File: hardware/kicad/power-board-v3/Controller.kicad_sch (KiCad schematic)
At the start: 1 part

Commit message: initial controller design
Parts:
- added C?: 10uF, symbol Device:C_Small
- added C? (x3): 100nF, symbol Device:C_Small
- added C?: 1uF, symbol Device:C_Small
- added J?: USB_BREAKOUT, Connector_PinHeader_2.54mm:PinHeader_1x03_P2.54mm_Vertical, symbol Connector_Generic:Conn_01x03
- added J?: SERIAL_PROGRAMMING, Connector_PinHeader_2.54mm:PinHeader_1x06_P2.54mm_Vertical, symbol Connector_Generic:Conn_01x06
- added J?: Conn_ARM_JTAG_SWD_10, Connector:Tag-Connect_TC2050-IDC-FP_2x05_P1.27mm_Vertical, symbol Connector:Conn_ARM_JTAG_SWD_10
- added JP?: JTAG_SELECT, symbol Jumper:SolderJumper_3_Open
- added Q? (x2): L8050QLT1G, Package_TO_SOT_SMD:SOT-23, symbol Device:Q_NPN_BEC
- added R? (x9): 10K, symbol Device:R_Small
- added SW?: BOOT, Button_Switch_SMD:SW_SPST_TL3342, symbol Switch:SW_Push
- added SW?: RESET, Button_Switch_SMD:SW_SPST_TL3342, symbol Switch:SW_Push
- added U?: ESP32-S3-MINI-1, Espressif:ESP32-S3-MINI-1, symbol Espressif:ESP32-S3-MINI-1
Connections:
- net +3.3v: now also C?.1, C?.1, J?.1 (VTref), R?.1, R?.2, R?.2, R?.2, U?.3 (3V3)
- net EN_FAN: now also U?.11 (GPIO7/TOUCH7/ADC1_CH6)
- net EN_LORA: now also U?.8 (GPIO4/TOUCH4/ADC1_CH3)
- net EN_RPI: now also U?.10 (GPIO6/TOUCH6/ADC1_CH5)
- net EN_SWARM: now also U?.9 (GPIO5/TOUCH5/ADC1_CH4)
- net GND: now also C?.2, C?.2, C?.2, C?.2, C?.2, J?.1 (Pin_1), J?.3 (GND), J?.5 (GND), J?.6 (Pin_6), J?.9 (GNDDetect), R?.1, R?.1, R?.1, SW?.1, SW?.1, U?.1 (GND), U?.2 (GND), U?.42 (GND), U?.43 (GND), U?.46 (GND), U?.47 (GND), U?.48 (GND), U?.49 (GND), U?.50 (GND), U?.51 (GND), U?.52 (GND), U?.53 (GND), U?.54 (GND), U?.55 (GND), U?.56 (GND), U?.57 (GND), U?.58 (GND), U?.59 (GND), U?.60 (GND), U?.61 (GND), U?.62 (GND), U?.63 (GND), U?.64 (GND), U?.65 (GND)
- net I2C_SDA: now reaches J3.2 (Pin_2)
- net I2C_SDA: now also U?.19 (GPIO15/U0RTS/ADC2_CH4/XTAL_32K_P)
- net I2C_SCL: now reaches J3.3 (Pin_3)
- net I2C_SCL: now also U?.20 (GPIO16/U0CTS/ADC2_CH5/XTAL_32K_NH5)
- new net: R?.2, U?.41 (GPIO45)
- new net: R?.2, U?.44 (GPIO46)
- new net: Q?.1 (B), R?.2 (x2)
- new net: JP?.1 (A), R?.2
- new net: JP?.3 (B), R?.1
- new net BOOT: C?.1, Q?.3 (C), R?.1, SW?.2, U?.4 (GPIO0/BOOT)
- new net CHIP_PU: C?.1, C?.1, J?.10 (~{RESET}), Q?.3 (C), R?.1, R?.2, SW?.2, U?.45 (EN)
- new net DTR: J?.1 (Pin_1), Q?.2 (E), R?.1
- new net JTAG_SEL: JP?.2 (C), U?.7 (GPIO3/TOUCH3/ADC1_CH2)
- new net MTCK: J?.4 (SWDCLK/TCK), U?.35 (MTCK/GPIO39/CLK_OUT3/SUBSPICS1)
- new net MTDI: J?.8 (NC/TDI), U?.37 (MTDI/GPIO41/CLK_OUT1)
- new net MTDO: J?.6 (SWO/TDO), U?.36 (MTDO/GPIO40/CLK_OUT2)
- new net MTMS: J?.2 (SWDIO/TMS), U?.38 (MTMS/GPIO42)
- new net RTS: J?.5 (Pin_5), Q?.2 (E), R?.1
- new net U0RXD: J?.3 (Pin_3), U?.40 (U0RXD/GPIO44/CLK_OUT2)
- new net U0TXD: J?.2 (Pin_2), U?.39 (U0TXD/GPIO43/CLK_OUT1)
- new net U1RXD: U?.21 (GPIO17/U1TXD/ADC2_CH6)
- new net U1TXD: U?.22 (GPIO18/U1RXD/ADC2_CH7/CLK_OUT3)
- new net USB_D+: J?.3 (Pin_3), U?.24 (GPIO20/U1CTS/ADC2_CH9/CLK_OUT1/USB_D+)
- new net USB_D-: J?.2 (Pin_2), U?.23 (GPIO19/U1RTS/ADC2_CH8/CLK_OUT2/USB_D-)
- new net VIN1_3V3_STATUS: U?.5 (GPIO1/TOUCH1/ADC1_CH0)
- new net VIN2_3V3_STATUS: U?.6 (GPIO2/TOUCH2/ADC1_CH1)
- no-connect marks 0 -> 18
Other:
- note added: "Boot Selection Button"
- note added: "Controller"
- note added: "Debugging Port"
- note added: "For Debugging"
- note added: "For Programming Port"
- note added: "JTAG Port"
- note added: "JTAG Select"
- note added: "Programming Port"
- note added: "RS485 Communication"
- note added: "Reset Button"
- note added: "Set EFUSE to only allow on-chip JTAG: - EFUSE_DIS_USB_JTAG = 1 - EFUSE_DIS_PAD_JTAG = 0"
- note added: "Strapping Pins: - GPIO0 = boot pin - GPIO45 = pull-down - GPIO46 = pull-down - GPIO03 = floating"
- note added: "TODO: Add protection circuit for rs-485"
- note added: "To RPi"
- note added: "To RS485 Converter"
- note added: "USB Breakout"
- moved on the sheet: J3

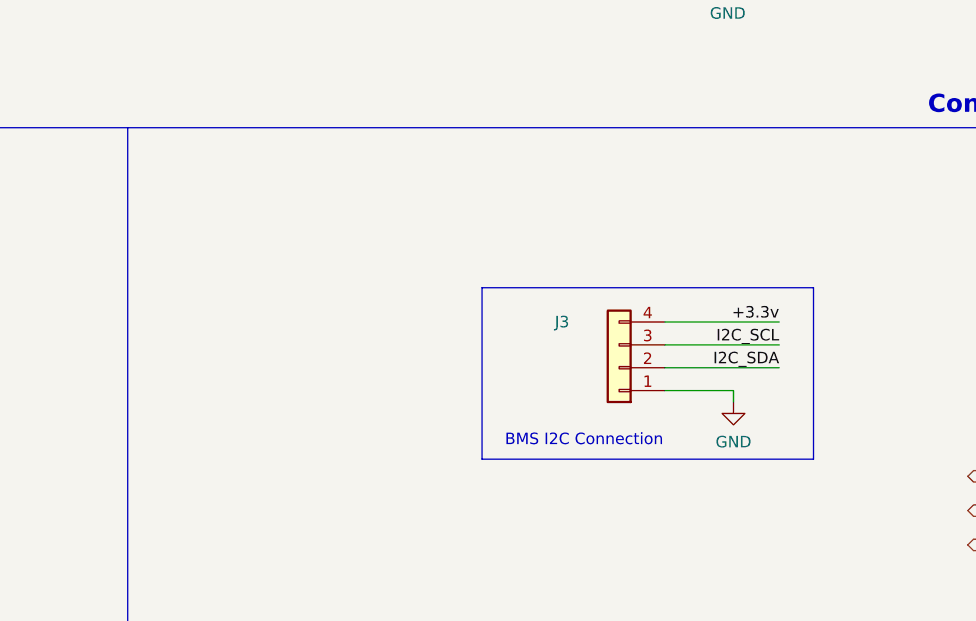
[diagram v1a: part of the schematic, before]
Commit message: change i2c interface
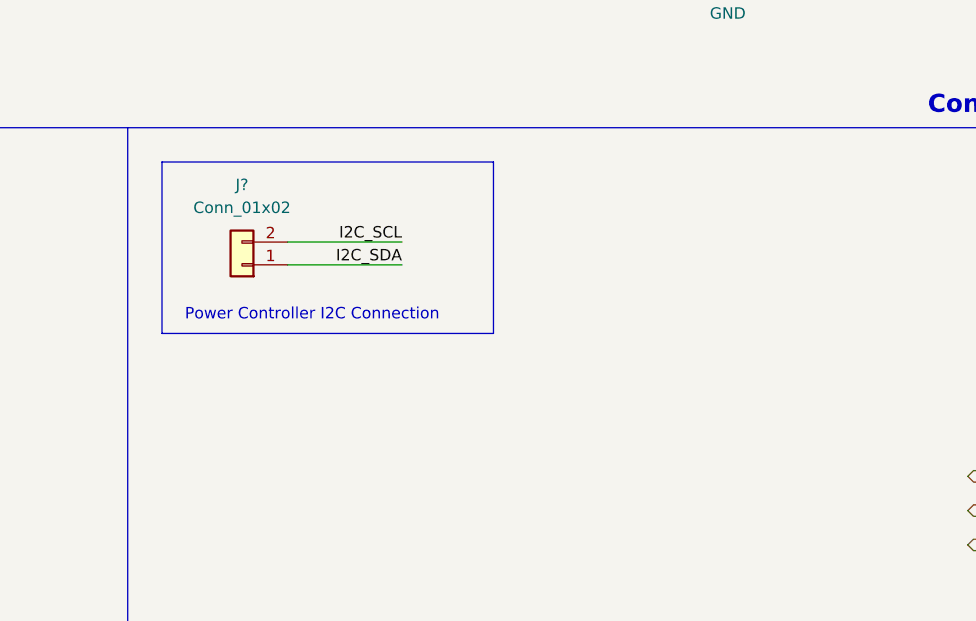
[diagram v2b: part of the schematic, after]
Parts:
- removed J3: ~, Connector_PinSocket_2.54mm:PinSocket_1x04_P2.54mm_Vertical, symbol Connector_Generic:Conn_01x04
- added J?: Conn_01x02, symbol Connector_Generic:Conn_01x02
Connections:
- net I2C_SCL: now also J?.2 (Pin_2)
- net I2C_SDA: now also J?.1 (Pin_1)
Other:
- note added: "Power Controller I2C Connection"
- note removed: "BMS I2C Connection"
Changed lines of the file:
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@@
     (stroke (width 0) (type default) (color 0 0 0 0))
   )
-  (polyline (pts (xy 187.96 142.24) (xy 151.13 142.24))
+  (polyline (pts (xy 152.4 128.27) (xy 115.57 128.27))
     (stroke (width 0) (type solid) (color 0 0 0 0))
   )
@@
     (stroke (width 0) (type default) (color 0 0 0 0))
   )
-  (polyline (pts (xy 187.96 123.19) (xy 187.96 142.24))
+  (polyline (pts (xy 152.4 109.22) (xy 152.4 128.27))
     (stroke (width 0) (type solid) (color 0 0 0 0))
   )
@@
     (stroke (width 0) (type default) (color 0 0 0 0))
   )
-  (wire (pts (xy 179.07 135.89) (xy 179.07 134.62))
-    (stroke (width 0) (type default) (color 0 0 0 0))
-  )
   (wire (pts (xy 53.975 171.45) (xy 26.035 171.45))
-    (stroke (width 0) (type default) (color 0 0 0 0))
-  )
-  (wire (pts (xy 171.45 127) (xy 184.15 127))
     (stroke (width 0) (type default) (color 0 0 0 0))
   )
@@
     (stroke (width 0) (type default) (color 0 0 0 0))
   )
-  (wire (pts (xy 171.45 132.08) (xy 184.15 132.08))
+  (wire (pts (xy 129.54 120.65) (xy 142.24 120.65))
     (stroke (width 0) (type default) (color 0 0 0 0))
   )
@@
     (stroke (width 0) (type default) (color 0 0 0 0))
   )
-  (polyline (pts (xy 151.13 123.19) (xy 151.13 142.24))
+  (polyline (pts (xy 115.57 109.22) (xy 115.57 128.27))
     (stroke (width 0) (type solid) (color 0 0 0 0))
   )
@@
     (stroke (width 0) (type default) (color 0 0 0 0))
   )
-  (wire (pts (xy 171.45 134.62) (xy 179.07 134.62))
-    (stroke (width 0) (type default) (color 0 0 0 0))
-  )
   (wire (pts (xy 237.49 71.755) (xy 247.65 71.755))
     (stroke (width 0) (type default) (color 0 0 0 0))
@@
     (stroke (width 0) (type default) (color 0 0 0 0))
   )
-  (wire (pts (xy 171.45 129.54) (xy 184.15 129.54))
+  (wire (pts (xy 129.54 118.11) (xy 142.24 118.11))
     (stroke (width 0) (type default) (color 0 0 0 0))
   )
@@
     (stroke (width 0) (type default) (color 0 0 0 0))
   )
-  (polyline (pts (xy 151.13 123.19) (xy 187.96 123.19))
+  (polyline (pts (xy 115.57 109.22) (xy 152.4 109.22))
     (stroke (width 0) (type solid) (color 0 0 0 0))
   )
@@
     (effects (font (size 1.27 1.27)) (justify left bottom))
   )
-  (text "BMS I2C Connection" (at 153.67 140.97 0)
+  (text "Power Controller I2C Connection" (at 118.11 127 0)
     (effects (font (size 1.27 1.27)) (justify left bottom))
   )
@@
     (effects (font (size 1.27 1.27)) (justify right bottom))
   )
-  (label "I2C_SDA" (at 184.15 132.08 180)
+  (label "I2C_SDA" (at 142.24 120.65 180)
     (effects (font (size 1.27 1.27)) (justify right bottom))
   )
@@
     (effects (font (size 1.27 1.27)) (justify left bottom))
   )
-  (label "I2C_SCL" (at 184.15 129.54 180)
+  (label "I2C_SCL" (at 142.24 118.11 180)
     (effects (font (size 1.27 1.27)) (justify right bottom))
   )
@@
   )
   (label "MTDO" (at 279.4 36.195 180)
-    (effects (font (size 1.27 1.27)) (justify right bottom))
-  )
-  (label "+3.3v" (at 184.15 127 180)
     (effects (font (size 1.27 1.27)) (justify right bottom))
   )
@@
     (pin "2")
   )
+  (symbol (lib_id "Connector_Generic:Conn_01x02") (at 124.46 120.65 180) (unit 1)
+    (in_bom yes) (on_board yes) (fields_autoplaced)
+    (property "Reference" "J?" (id 0) (at 124.46 111.76 0))
+    (property "Value" "Conn_01x02" (id 1) (at 124.46 114.3 0))
+    (property "Footprint" "" (id 2) (at 124.46 120.65 0)
+      (effects (font (size 1.27 1.27)) hide)
+    )
+    (property "Datasheet" "~" (id 3) (at 124.46 120.65 0)
+      (effects (font (size 1.27 1.27)) hide)
+    )
+    (pin "1")
+    (pin "2")
+  )
   (symbol (lib_id "Connector:Conn_ARM_JTAG_SWD_10") (at 257.81 33.655 0) (unit 1)
     (in_bom yes) (on_board yes) (fields_autoplaced)
@@
     (pin "1")
   )
-  (symbol (lib_id "power:GND") (at 179.07 135.89 0) (unit 1)
-    (in_bom yes) (on_board yes)
-    (property "Reference" "#PWR?" (id 0) (at 179.07 142.24 0)
-      (effects (font (size 1.27 1.27)) hide)
-    )
-    (property "Value" "GND" (id 1) (at 179.07 140.335 0))
-    (property "Footprint" "" (id 2) (at 179.07 135.89 0)
-      (effects (font (size 1.27 1.27)) hide)
-    )
-    (property "Datasheet" "" (id 3) (at 179.07 135.89 0)
-      (effects (font (size 1.27 1.27)) hide)
-    )
-    (pin "1")
-  )
   (symbol (lib_id "Device:R_Small") (at 33.655 29.21 90) (unit 1)
     (in_bom yes) (on_board yes)
@@
     (pin "2")
   )
-  (symbol (lib_id "Connector_Generic:Conn_01x04") (at 166.37 132.08 180) (unit 1)
-    (in_bom yes) (on_board yes)
-    (property "Reference" "J3" (id 0) (at 160.02 127 0))
-    (property "Value" "~" (id 1) (at 158.75 129.54 0))
-    (property "Footprint" "Connector_PinSocket_2.54mm:PinSocket_1x04_P2.54mm_Vertical" (id 2) (at 166.37 132.08 0)
-      (effects (font (size 1.27 1.27)) hide)
-    )
-    (property "Datasheet" "~" (id 3) (at 166.37 132.08 0)
-      (effects (font (size 1.27 1.27)) hide)
-    )
-    (pin "1")
-    (pin "2")
-    (pin "3")
-    (pin "4")
-  )
   (symbol (lib_id "power:GND") (at 178.435 87.63 0) (unit 1)
